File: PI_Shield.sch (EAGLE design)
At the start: 67 parts, among them Q1 220mA/50V/3.5Ω, Q3 220mA/50V/3.5Ω, Q4 220mA/50V/3.5Ω, Q5 2.5A/30V/105mΩ, U1 MAX1136EUA-T, U2 AZ1117EH-3.3TRG1, Y1 ECS-80-S-4X

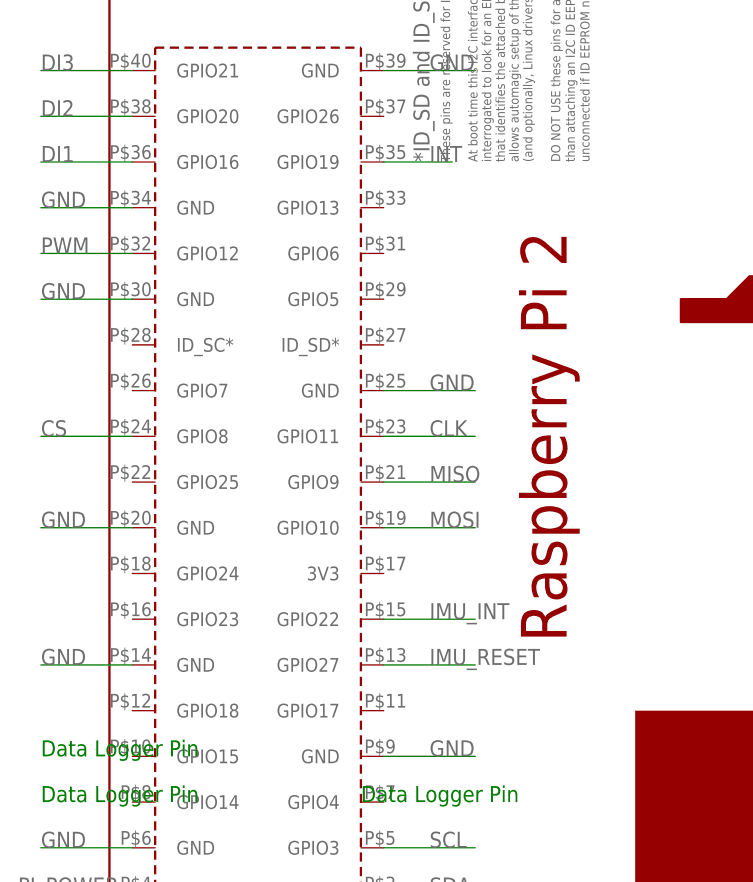
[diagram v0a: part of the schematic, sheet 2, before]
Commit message: Most of Changes done, need to impedance match
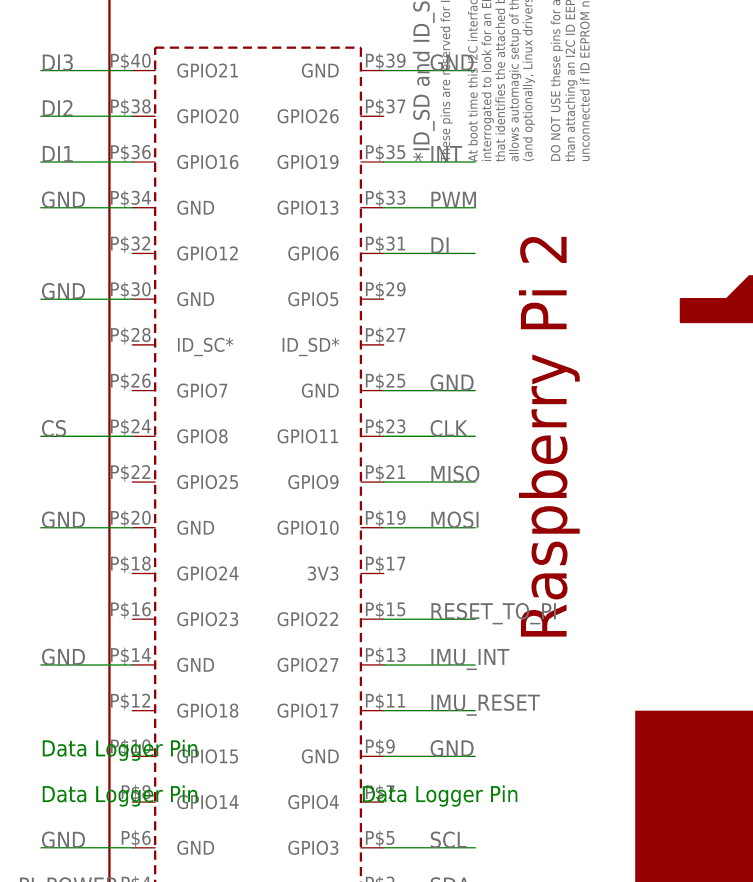
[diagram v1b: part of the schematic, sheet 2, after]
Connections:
- net DI: now also PCB1.GPIO6
- net IMU_INT: now also PCB1.GPIO27; no longer PCB1.GPIO22
- net IMU_RESET: now also PCB1.GPIO17; no longer PCB1.GPIO27
- net PWM: now also PCB1.GPIO13; no longer PCB1.GPIO12
- net RESET_TO_PI: now also PCB1.GPIO22
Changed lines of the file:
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@@
 </segment>
 <segment>
-<pinref part="PCB1" gate="G$1" pin="GPIO27"/>
-<wire x1="45.72" y1="50.8" x2="55.88" y2="50.8" width="0.1524" layer="91"/>
-<label x="50.8" y="50.8" size="1.778" layer="95"/>
+<pinref part="PCB1" gate="G$1" pin="GPIO17"/>
+<wire x1="45.72" y1="45.72" x2="55.88" y2="45.72" width="0.1524" layer="91"/>
+<label x="50.8" y="45.72" size="1.778" layer="95"/>
 </segment>
 </net>
@@
 </segment>
 <segment>
-<pinref part="PCB1" gate="G$1" pin="GPIO22"/>
-<wire x1="45.72" y1="55.88" x2="55.88" y2="55.88" width="0.1524" layer="91"/>
-<label x="50.8" y="55.88" size="1.778" layer="95"/>
+<pinref part="PCB1" gate="G$1" pin="GPIO27"/>
+<wire x1="45.72" y1="50.8" x2="55.88" y2="50.8" width="0.1524" layer="91"/>
+<label x="50.8" y="50.8" size="1.778" layer="95"/>
 </segment>
 </net>
@@
 <segment>
 <pinref part="PCB1" gate="G$1" pin="GPIO19"/>
-<wire x1="45.72" y1="106.68" x2="53.34" y2="106.68" width="0.1524" layer="91"/>
+<wire x1="45.72" y1="106.68" x2="55.88" y2="106.68" width="0.1524" layer="91"/>
 <label x="50.8" y="106.68" size="1.778" layer="95"/>
 </segment>
@@
 <pinref part="R20" gate="G$1" pin="1"/>
 <wire x1="124.46" y1="15.24" x2="124.46" y2="17.78" width="0.1524" layer="91"/>
+</segment>
+<segment>
+<pinref part="PCB1" gate="G$1" pin="GPIO6"/>
+<wire x1="45.72" y1="96.52" x2="55.88" y2="96.52" width="0.1524" layer="91"/>
+<label x="50.8" y="96.52" size="1.778" layer="95"/>
 </segment>
 </net>
@@
 </segment>
 <segment>
-<pinref part="PCB1" gate="G$1" pin="GPIO12"/>
-<wire x1="17.78" y1="96.52" x2="7.62" y2="96.52" width="0.1524" layer="91"/>
-<label x="7.62" y="96.52" size="1.778" layer="95"/>
+<pinref part="PCB1" gate="G$1" pin="GPIO13"/>
+<wire x1="45.72" y1="101.6" x2="55.88" y2="101.6" width="0.1524" layer="91"/>
+<label x="50.8" y="101.6" size="1.778" layer="95"/>
 </segment>
 </net>
@@
 </segment>
 </net>
+<net name="RESET_TO_PI" class="0">
+<segment>
+<pinref part="PCB1" gate="G$1" pin="GPIO22"/>
+<wire x1="45.72" y1="55.88" x2="55.88" y2="55.88" width="0.1524" layer="91"/>
+<label x="50.8" y="55.88" size="1.778" layer="95"/>
+</segment>
+</net>

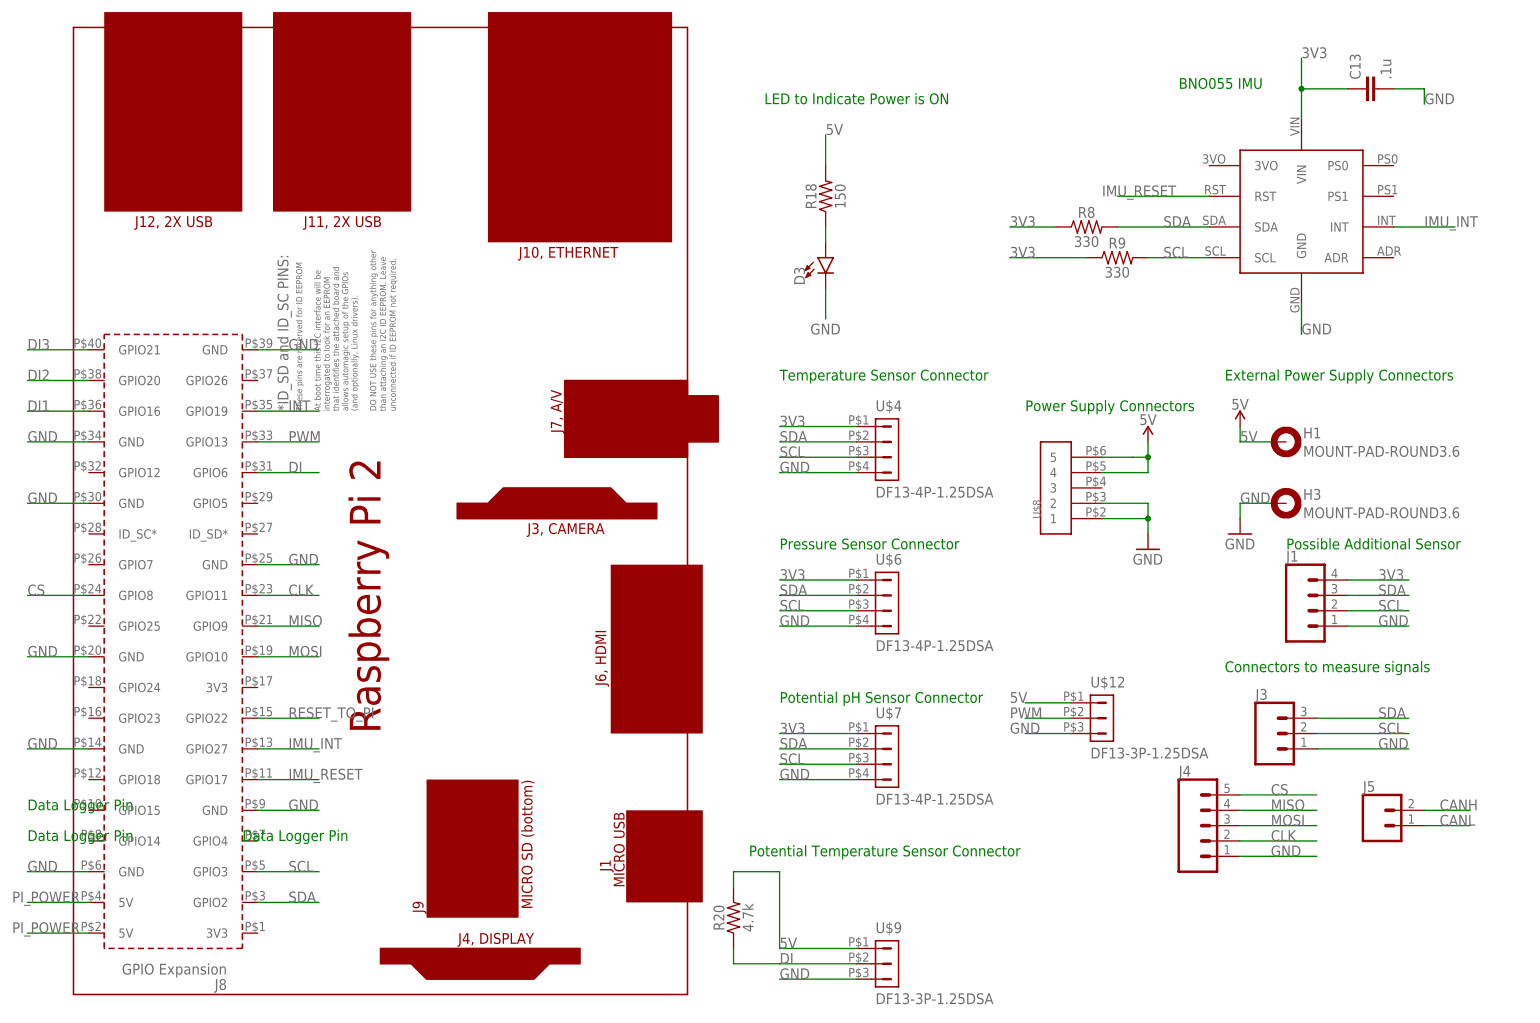
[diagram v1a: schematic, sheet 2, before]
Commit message: Added Silkscreen Text
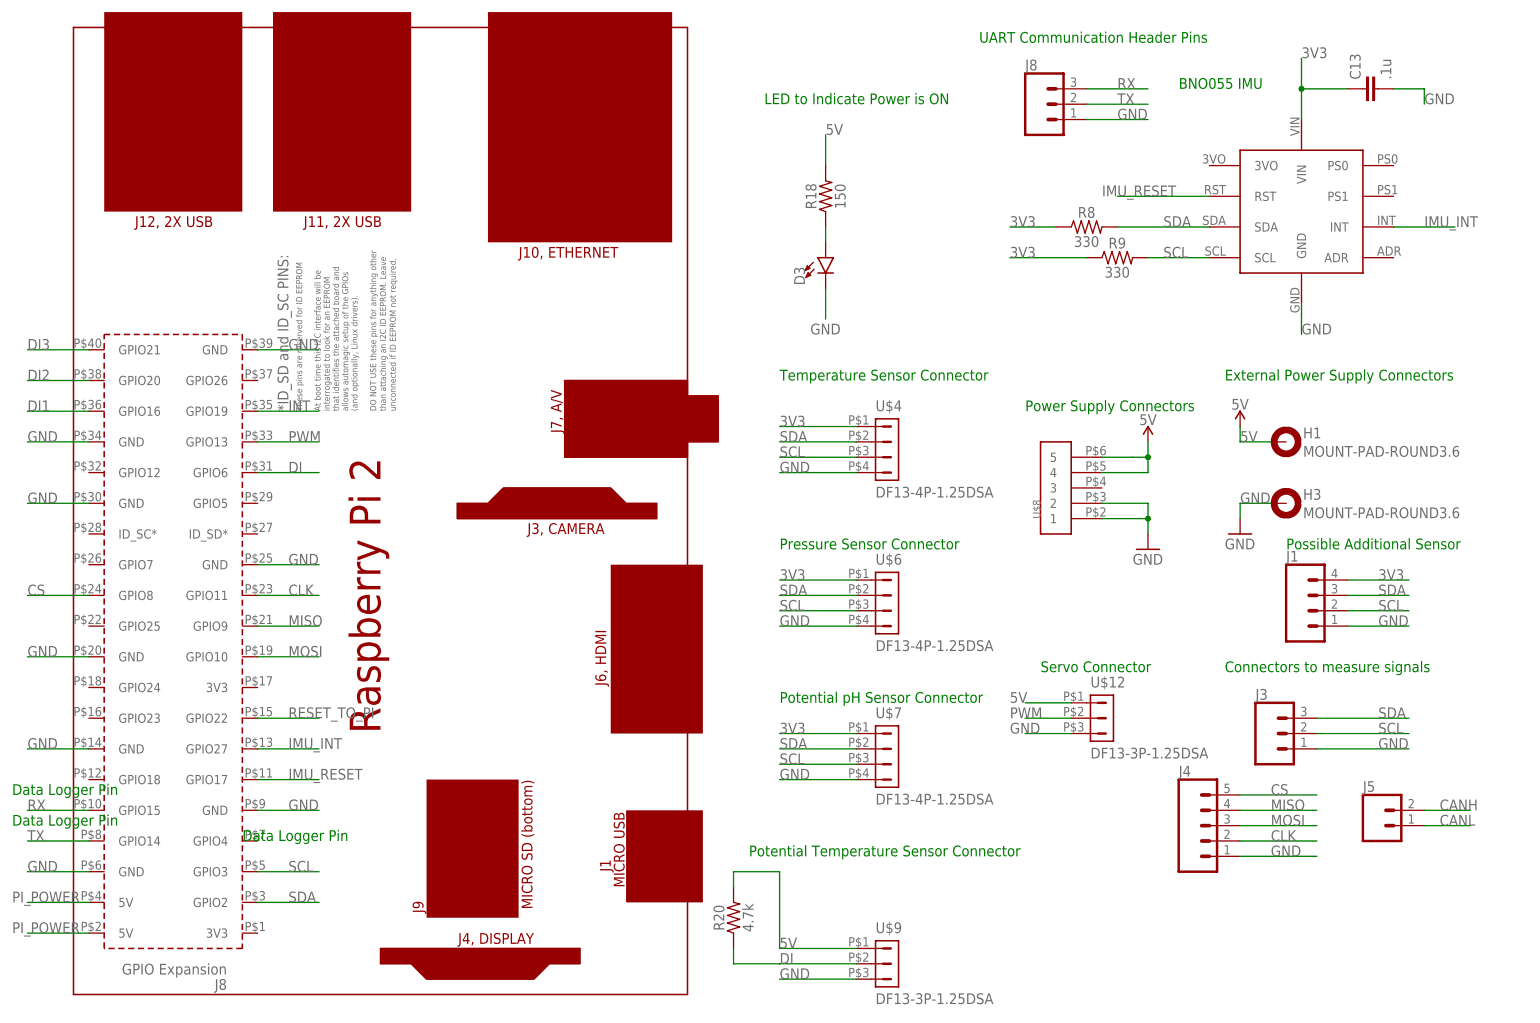
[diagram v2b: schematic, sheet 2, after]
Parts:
- added J8: (no value), SparkFun-Connectors:CONN_03
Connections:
- new net RX: J8.3, PCB1.GPIO15
- new net TX: J8.2, PCB1.GPIO14
- net 5V: now also U$11.1; no longer U$11.2
- net AIN: now also U$11.2; no longer U$11.1
- net GND: now also J8.1
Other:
- note added: "Servo Connector"
- note added: "UART Communication Header Pins"
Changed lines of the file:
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@@
 <part name="J6" library="SparkFun-Connectors" deviceset="CONN_02" device=""/>
 <part name="J7" library="SparkFun-Connectors" deviceset="CONN_02" device=""/>
+<part name="J8" library="SparkFun-Connectors" library_urn="urn:adsk.eagle:library:513" deviceset="CONN_03" device="" package3d_urn="urn:adsk.eagle:package:38063/1"/>
 </parts>
 <sheets>
@@
 <text x="127" y="33.02" size="1.778" layer="91">Potential Temperature Sensor Connector</text>
 <text x="172.72" y="106.68" size="1.778" layer="91">Power Supply Connectors</text>
-<text x="7.62" y="40.64" size="1.778" layer="91">Data Logger Pin</text>
-<text x="7.62" y="35.56" size="1.778" layer="91">Data Logger Pin</text>
+<text x="5.08" y="43.18" size="1.778" layer="91">Data Logger Pin</text>
+<text x="5.08" y="38.1" size="1.778" layer="91">Data Logger Pin</text>
 <text x="43.18" y="35.56" size="1.778" layer="91">Data Logger Pin</text>
 <text x="215.9" y="83.82" size="1.778" layer="91">Possible Additional Sensor</text>
+<text x="165.1" y="167.64" size="1.778" layer="91">UART Communication Header Pins</text>
+<text x="175.26" y="63.5" size="1.778" layer="91">Servo Connector</text>
 </plain>
 <instances>
@@
 <attribute name="VALUE" x="215.9" y="66.294" size="1.778" layer="96" font="vector"/>
 <attribute name="NAME" x="215.9" y="81.788" size="1.778" layer="95" font="vector"/>
+</instance>
+<instance part="J8" gate="J$1" x="175.26" y="157.48" smashed="yes">
+<attribute name="VALUE" x="172.72" y="150.114" size="1.778" layer="96" font="vector"/>
+<attribute name="NAME" x="172.72" y="163.068" size="1.778" layer="95" font="vector"/>
 </instance>
 </instances>
@@
 <wire x1="226.06" y1="71.12" x2="236.22" y2="71.12" width="0.1524" layer="91"/>
 <label x="231.14" y="71.12" size="1.778" layer="95"/>
+</segment>
+<segment>
+<pinref part="J8" gate="J$1" pin="1"/>
+<wire x1="182.88" y1="154.94" x2="193.04" y2="154.94" width="0.1524" layer="91"/>
+<label x="187.96" y="154.94" size="1.778" layer="95"/>
 </segment>
 </net>
@@
 <wire x1="45.72" y1="55.88" x2="55.88" y2="55.88" width="0.1524" layer="91"/>
 <label x="50.8" y="55.88" size="1.778" layer="95"/>
+</segment>
+</net>
+<net name="TX" class="0">
+<segment>
+<pinref part="PCB1" gate="G$1" pin="GPIO14"/>
+<wire x1="17.78" y1="35.56" x2="7.62" y2="35.56" width="0.1524" layer="91"/>
+<label x="7.62" y="35.56" size="1.778" layer="95"/>
+</segment>
+<segment>
+<pinref part="J8" gate="J$1" pin="2"/>
+<wire x1="182.88" y1="157.48" x2="193.04" y2="157.48" width="0.1524" layer="91"/>
+<label x="187.96" y="157.48" size="1.778" layer="95"/>
+</segment>
+</net>
+<net name="RX" class="0">
+<segment>
+<pinref part="PCB1" gate="G$1" pin="GPIO15"/>
+<wire x1="17.78" y1="40.64" x2="7.62" y2="40.64" width="0.1524" layer="91"/>
+<label x="7.62" y="40.64" size="1.778" layer="95"/>
+</segment>
+<segment>
+<pinref part="J8" gate="J$1" pin="3"/>
+<wire x1="182.88" y1="160.02" x2="193.04" y2="160.02" width="0.1524" layer="91"/>
+<label x="187.96" y="160.02" size="1.778" layer="95"/>
 </segment>
 </net>
@@
 <net name="5V" class="0">
 <segment>
-<wire x1="38.1" y1="142.24" x2="50.8" y2="142.24" width="0.1524" layer="91"/>
-<label x="48.26" y="142.24" size="1.778" layer="95"/>
-<pinref part="U$11" gate="G$1" pin="2"/>
-</segment>
-<segment>
 <pinref part="U1" gate="A" pin="VDD"/>
 <wire x1="144.78" y1="147.32" x2="149.86" y2="147.32" width="0.1524" layer="91"/>
@@
 <label x="33.02" y="106.68" size="1.778" layer="95"/>
 </segment>
+<segment>
+<pinref part="U$11" gate="G$1" pin="1"/>
+<wire x1="38.1" y1="139.7" x2="50.8" y2="139.7" width="0.1524" layer="91"/>
+<label x="48.26" y="139.7" size="1.778" layer="95"/>
+</segment>
 </net>
 <net name="SDA" class="0">
@@
 <net name="AIN" class="0">
 <segment>
-<wire x1="38.1" y1="139.7" x2="58.42" y2="139.7" width="0.1524" layer="91"/>
-<wire x1="58.42" y1="139.7" x2="58.42" y2="147.32" width="0.1524" layer="91"/>
 <pinref part="U1" gate="A" pin="AIN0"/>
 <wire x1="58.42" y1="147.32" x2="78.74" y2="147.32" width="0.1524" layer="91"/>
-<label x="48.26" y="139.7" size="1.778" layer="95"/>
-<pinref part="U$11" gate="G$1" pin="1"/>
-</segment>
-</net>
+<pinref part="U$11" gate="G$1" pin="2"/>
+<wire x1="38.1" y1="142.24" x2="58.42" y2="142.24" width="0.1524" layer="91"/>
+<wire x1="58.42" y1="142.24" x2="58.42" y2="147.32" width="0.1524" layer="91"/>
+<label x="48.26" y="142.24" size="1.778" layer="95"/>
+</segment>
+</net>

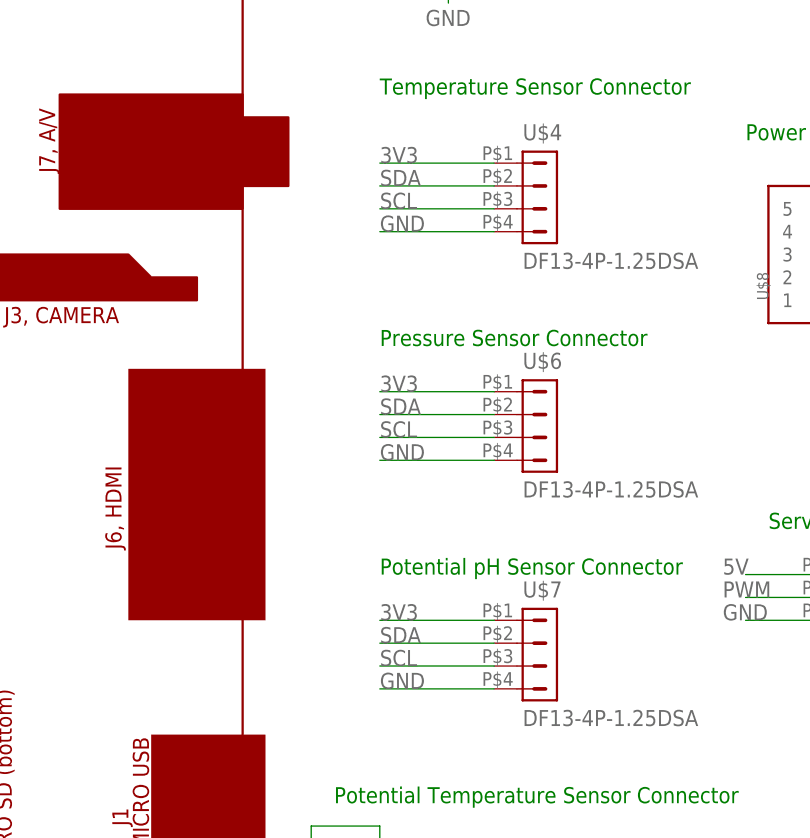
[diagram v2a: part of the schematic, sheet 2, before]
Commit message: Fixed connector inputs for sensors to match blue robotics website
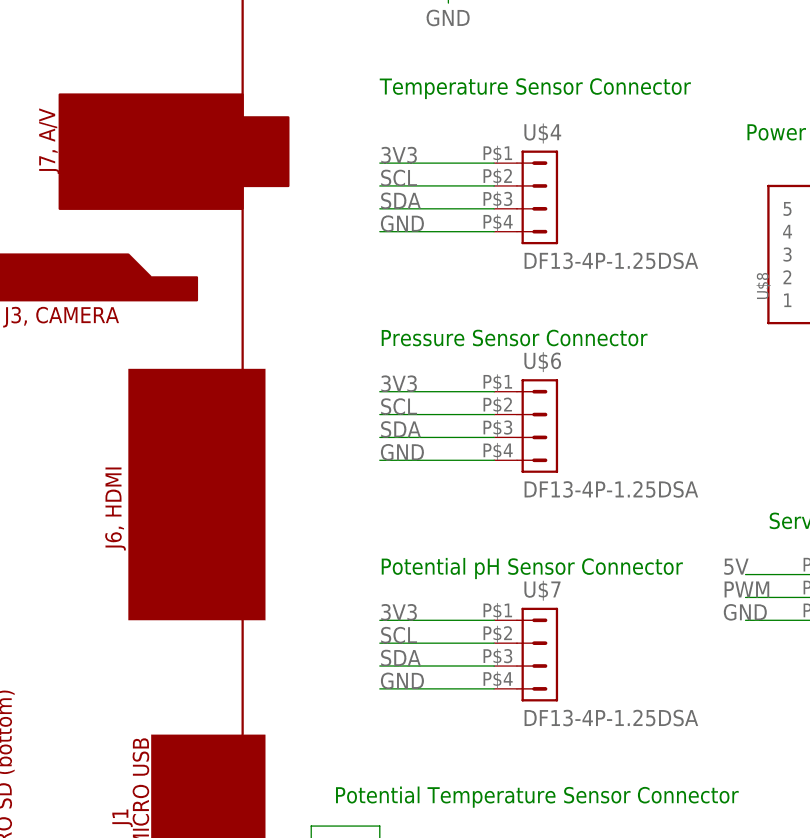
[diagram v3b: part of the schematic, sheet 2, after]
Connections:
- net SCL: now also U$4.2, U$6.2, U$7.2; no longer U$4.3, U$6.3, U$7.3
- net SDA: now also U$4.3, U$6.3, U$7.3; no longer U$4.2, U$6.2, U$7.2
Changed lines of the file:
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@@
 <?xml version="1.0" encoding="utf-8"?>
 <!DOCTYPE eagle SYSTEM "eagle.dtd">
-<eagle version="9.2.2">
+<eagle version="9.1.3">
 <drawing>
 <settings>
@@
 </segment>
 <segment>
-<pinref part="U$4" gate="G$1" pin="2"/>
-<wire x1="144.78" y1="101.6" x2="132.08" y2="101.6" width="0.1524" layer="91"/>
-<label x="132.08" y="101.6" size="1.778" layer="95"/>
-</segment>
-<segment>
-<pinref part="U$6" gate="G$1" pin="2"/>
-<wire x1="144.78" y1="76.2" x2="132.08" y2="76.2" width="0.1524" layer="91"/>
-<label x="132.08" y="76.2" size="1.778" layer="95"/>
-</segment>
-<segment>
-<pinref part="U$7" gate="G$1" pin="2"/>
-<wire x1="144.78" y1="50.8" x2="132.08" y2="50.8" width="0.1524" layer="91"/>
-<label x="132.08" y="50.8" size="1.778" layer="95"/>
-</segment>
-<segment>
 <pinref part="J1" gate="G$1" pin="3"/>
 <wire x1="226.06" y1="76.2" x2="236.22" y2="76.2" width="0.1524" layer="91"/>
 <label x="231.14" y="76.2" size="1.778" layer="95"/>
+</segment>
+<segment>
+<pinref part="U$4" gate="G$1" pin="3"/>
+<wire x1="144.78" y1="99.06" x2="132.08" y2="99.06" width="0.1524" layer="91"/>
+<label x="132.08" y="99.06" size="1.778" layer="95"/>
+</segment>
+<segment>
+<pinref part="U$6" gate="G$1" pin="3"/>
+<wire x1="144.78" y1="73.66" x2="132.08" y2="73.66" width="0.1524" layer="91"/>
+<label x="132.08" y="73.66" size="1.778" layer="95"/>
+</segment>
+<segment>
+<pinref part="U$7" gate="G$1" pin="3"/>
+<wire x1="144.78" y1="48.26" x2="132.08" y2="48.26" width="0.1524" layer="91"/>
+<label x="132.08" y="48.26" size="1.778" layer="95"/>
 </segment>
 </net>
@@
 </segment>
 <segment>
-<pinref part="U$4" gate="G$1" pin="3"/>
-<wire x1="144.78" y1="99.06" x2="132.08" y2="99.06" width="0.1524" layer="91"/>
-<label x="132.08" y="99.06" size="1.778" layer="95"/>
-</segment>
-<segment>
-<pinref part="U$6" gate="G$1" pin="3"/>
-<wire x1="144.78" y1="73.66" x2="132.08" y2="73.66" width="0.1524" layer="91"/>
-<label x="132.08" y="73.66" size="1.778" layer="95"/>
-</segment>
-<segment>
-<pinref part="U$7" gate="G$1" pin="3"/>
-<wire x1="144.78" y1="48.26" x2="132.08" y2="48.26" width="0.1524" layer="91"/>
-<label x="132.08" y="48.26" size="1.778" layer="95"/>
-</segment>
-<segment>
 <pinref part="J1" gate="G$1" pin="2"/>
 <wire x1="226.06" y1="73.66" x2="236.22" y2="73.66" width="0.1524" layer="91"/>
 <label x="231.14" y="73.66" size="1.778" layer="95"/>
 </segment>
-</net>
+<segment>
+<pinref part="U$4" gate="G$1" pin="2"/>
+<wire x1="144.78" y1="101.6" x2="132.08" y2="101.6" width="0.1524" layer="91"/>
+<label x="132.08" y="101.6" size="1.778" layer="95"/>
+</segment>
+<segment>
+<pinref part="U$6" gate="G$1" pin="2"/>
+<wire x1="144.78" y1="76.2" x2="132.08" y2="76.2" width="0.1524" layer="91"/>
+<label x="132.08" y="76.2" size="1.778" layer="95"/>
+</segment>
+<segment>
+<pinref part="U$7" gate="G$1" pin="2"/>
+<wire x1="144.78" y1="50.8" x2="132.08" y2="50.8" width="0.1524" layer="91"/>
+<label x="132.08" y="50.8" size="1.778" layer="95"/>
+</segment>
+</net>
